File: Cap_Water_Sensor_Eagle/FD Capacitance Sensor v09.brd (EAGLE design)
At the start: 35.1 x 27.6 mm, 17 parts, among them U1 NTS4101PT1, U2 TLC555CD

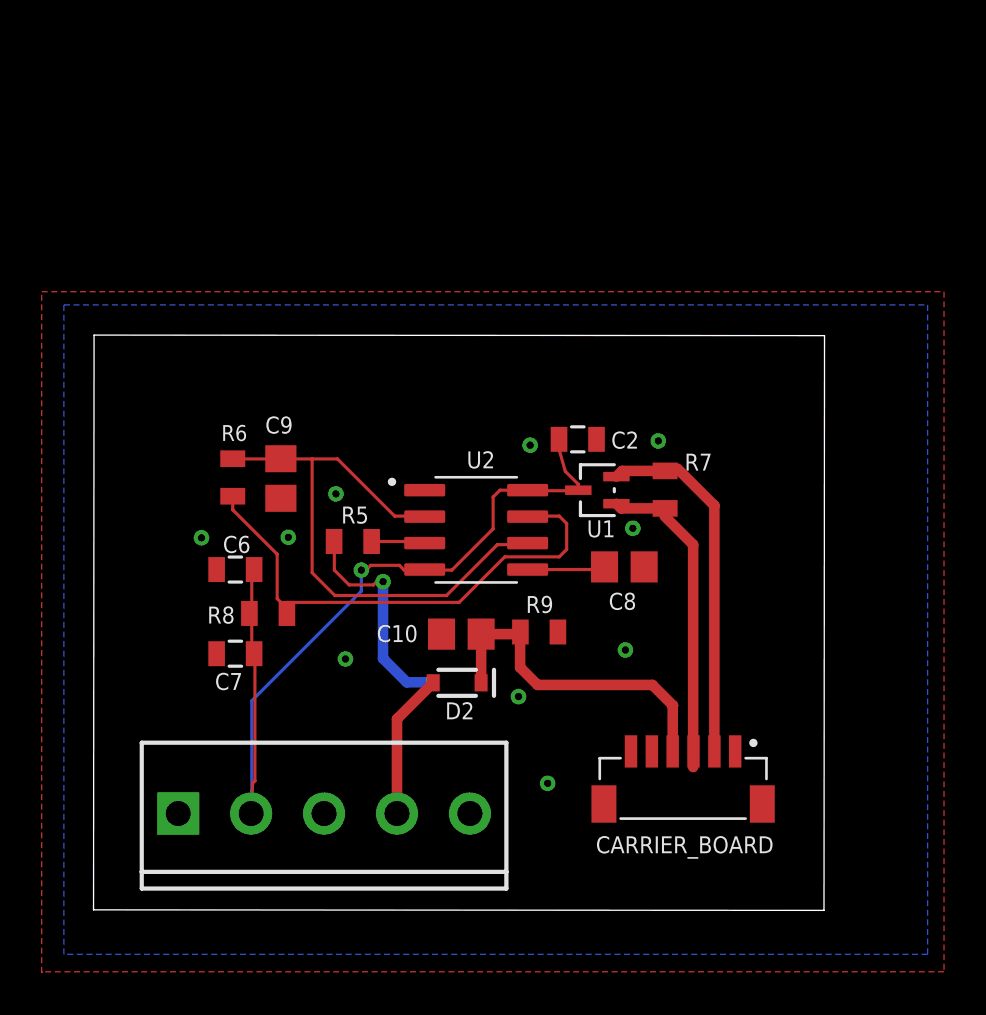
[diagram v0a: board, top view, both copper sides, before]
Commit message: Version 9 with board dimensions
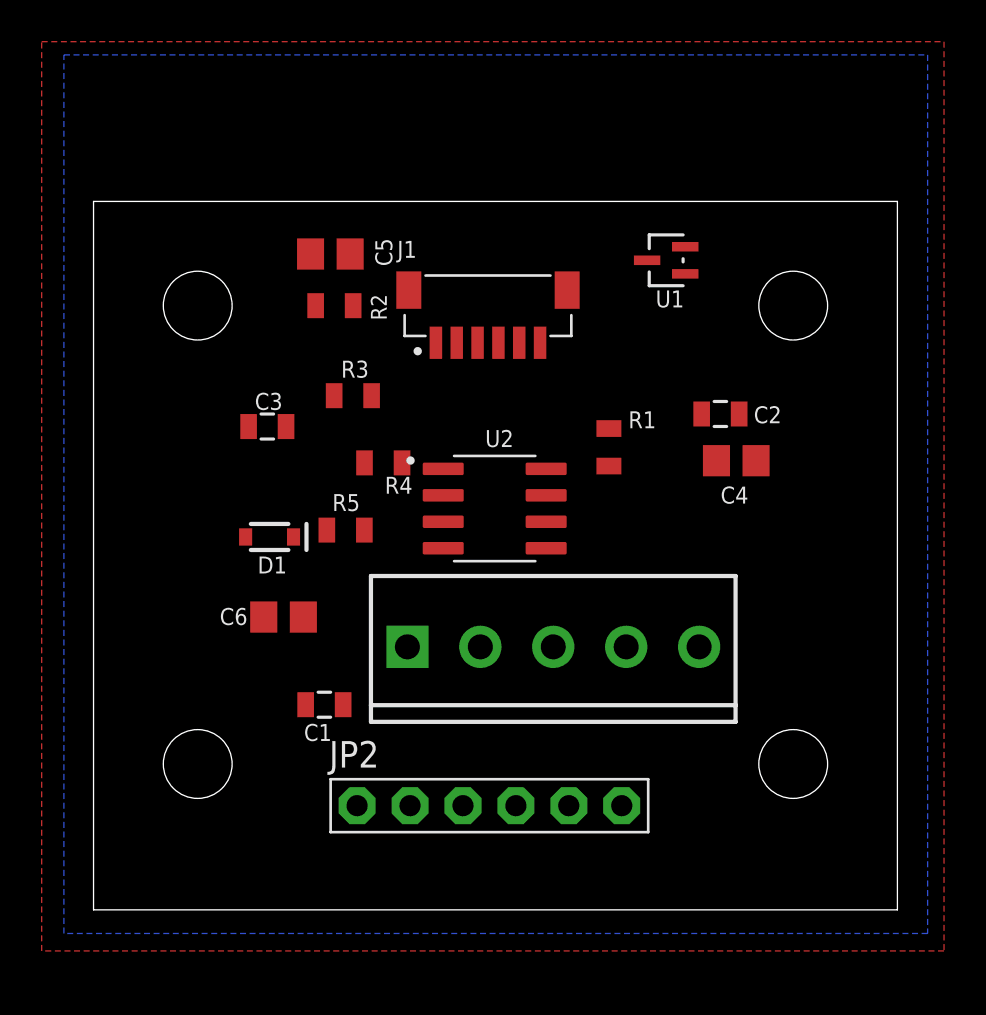
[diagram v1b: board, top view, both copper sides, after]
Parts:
- removed C10: 1uF, rcl:C0805
- removed C7: 0.1uF, Custom Components:0805@1
- removed C8: 10nf, rcl:C0805
- removed C9: 470pf, rcl:C0805
- removed CARRIER_BOARD: BM06B-SRSS-TBT(LF)(SN), Custom Components:JST_BM06B-SRSS-TB(LF)(SN)
- removed D2: 250mA/100V, Custom Components:SOD-323
- removed FRAME1: FRAME-LETTERNO_PACKAGE, SparkFun-Aesthetics:DUMMY
- removed R6: 1k, Custom Components:0805
- removed R7: 100k, Custom Components:0805
- removed R8: 330, Custom Components:0805
- removed R9: 1M, Custom Components:0805
- added C1: 0.1uF, Custom Components:0805@1
- added C3: 10nF, Custom Components:0805@1
- added C4: 10nf, rcl:C0805
- added C5: 470pf, rcl:C0805
- added D1: 250mA/100V, Custom Components:SOD-323
- added J2: (no value), SparkFun-Connectors:SCREWTERMINAL-3.5MM-5
- added JP2: (no value), adafruit:1X06-BIG
- added R1: 100k, Custom Components:0805
- added R2: 1k, Custom Components:0805
- added R3: 10k, Custom Components:0805
- added R4: 330, Custom Components:0805
- added U$1, U$2, U$3, U$4: STAND-OFF, SparkFun-Hardware:STAND-OFF
- C6: value 10nF -> 1uF; device Custom Components:0805@1 -> rcl:C0805
- J1: value (none) -> BM06B-SRSS-TBT(LF)(SN); device SparkFun-Connectors:SCREWTERMINAL-3.5MM-5 -> Custom Components:JST_BM06B-SRSS-TB(LF)(SN)
- R5: value 10k -> 1M
- moved J1 29.2 mm to (18.9, 29.7)
- moved U1 11.5 mm to (27.5, 31.2)
- moved C2 6.95 mm to (30.1, 23.8)
- moved C6 3.25 mm to (9.12, 14.1), turned to 0 degrees
- moved U2 1.36 mm to (19.3, 19.3)
- moved R5 0.65 mm to (12.1, 18.2)
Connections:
- new net N$2: JP2.3
- new net N$3: JP2.2
- new net N$4: JP2.4
- new net N$6: JP2.5
- net !EN: now also J1.3, R1.1; no longer CARRIER_BOARD.3, R7.1
- net +3V3: now also J1.2, R1.2; no longer CARRIER_BOARD.2, R7.2
- net GND: now also C1.2, C3.2, C4.1, C5.1, C6.1, J1.S1, J1.S2, J2.1, JP2.1, R5.1; no longer C10.1, C6.2, C7.2, C8.1, C9.1, CARRIER_BOARD.1, CARRIER_BOARD.S1, CARRIER_BOARD.S2, R9.1
- net N$1: now also C4.2; no longer C8.2
- net N$5: now also R3.1; no longer R5.1
- net N$8: now also C5.2, R2.1; no longer C9.2, R6.1
- net N$9: now also R2.2, R4.1; no longer R6.2, R8.1
- net NC: now also J1.6; no longer CARRIER_BOARD.6
- net OUTPUT1: now also C6.2, D1.C, J1.4, R5.2; no longer C10.2, CARRIER_BOARD.4, D2.C, R9.2
- net OUTPUT2: now also J1.5; no longer CARRIER_BOARD.5
- net SENSOR1: now also D1.A, J2.4, R3.2; no longer D2.A, J1.4, R5.2
- net SENSOR2: now also J2.5; no longer J1.5
- net SHEILD: now also J2.3; no longer J1.3
- net VCC: now also C1.1, C3.1, J2.2, R4.2; no longer C6.1, C7.1, J1.2, R8.2
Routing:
- net VCC: track 41.8 -> 0.61 mm, vias 1 -> 0
- net N$8: track 27.7 -> 0.26 mm
- net N$9: track 25.0 -> 0.03 mm
- net SENSOR1: track 17.6 -> 0.00 mm, vias 1 -> 0
- net +3V3: track 17.5 -> 0.07 mm
- net !EN: track 16.3 -> 0.03 mm
- net OUTPUT1: track 16.5 -> 0.41 mm
- net N$1: track 3.79 -> 0.03 mm
- net N$5: track 2.58 -> 0.00 mm
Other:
- board size 35.1 x 27.6 mm -> 38.6 x 34 mm

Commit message: Added Auto Routed Lines
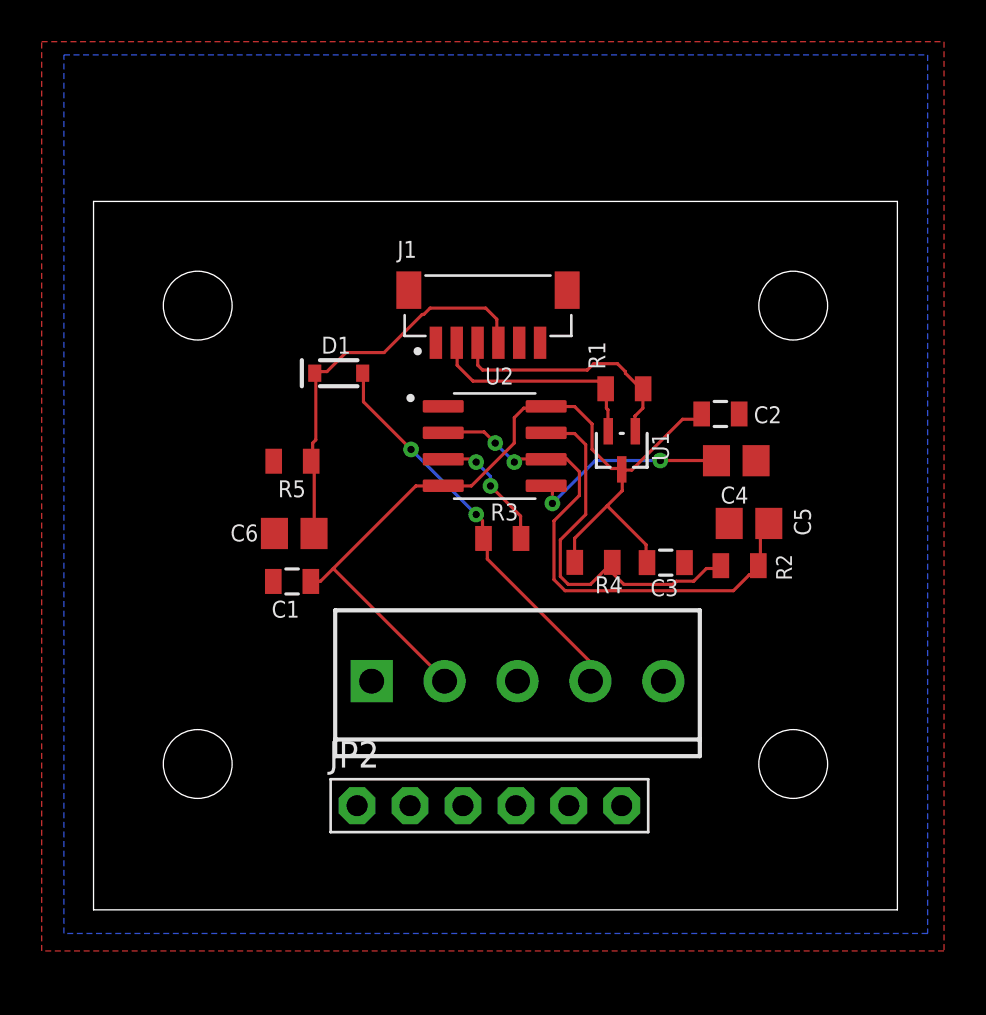
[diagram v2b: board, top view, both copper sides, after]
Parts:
- moved C5 23.9 mm to (31.5, 18.5)
- moved R2 23.1 mm to (31.0, 16.5)
- moved C3 20.2 mm to (27.5, 16.7), turned to 0 degrees
- moved R4 11.2 mm to (24.0, 16.7)
- moved R3 9.92 mm to (19.6, 17.8)
- moved U1 9.37 mm to (25.4, 22.1), turned to 180 degrees
- moved D1 8.53 mm to (11.8, 25.8), turned to 0 degrees
- moved C1 6.12 mm to (9.53, 15.8)
- moved R5 4.17 mm to (9.55, 21.5), turned to 0 degrees
- moved C6 4.04 mm to (9.63, 18.1)
- moved U2 3.00 mm to (19.3, 22.3)
- moved R1 2.91 mm to (25.5, 25.0), turned to 180 degrees
- moved J2 2.38 mm to (13.3, 11.0)
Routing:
- net VCC: track 0.61 -> 43.7 mm
- net N$8: track 0.26 -> 26.2 mm, vias 0 -> 2
- net SENSOR1: track 0.00 -> 19.3 mm, vias 0 -> 2
- net OUTPUT1: track 0.41 -> 19.5 mm
- net N$9: track 0.03 -> 18.4 mm
- net !EN: track 0.03 -> 12.0 mm
- net +3V3: track 0.07 -> 10.8 mm
- net N$1: track 0.03 -> 9.76 mm, vias 0 -> 2
- net N$5: track 0.00 -> 6.21 mm, vias 0 -> 2

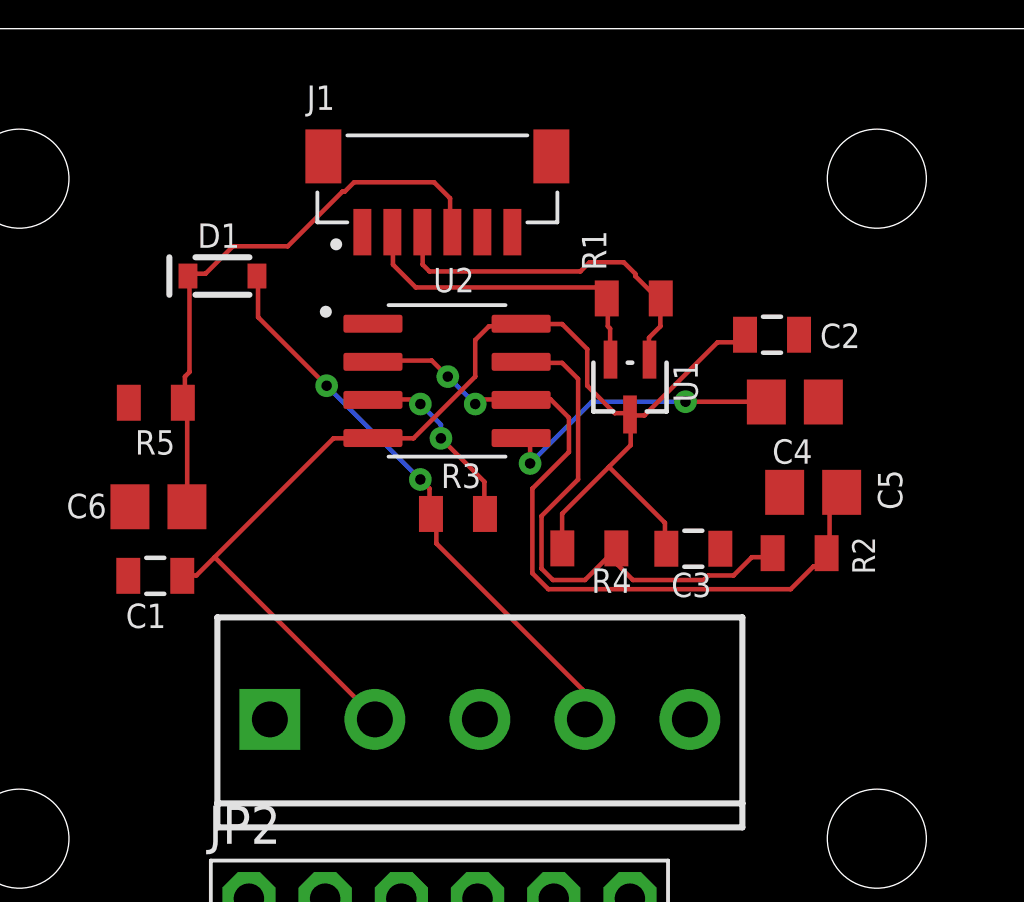
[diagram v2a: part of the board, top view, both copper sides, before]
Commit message: Removed Auto Route
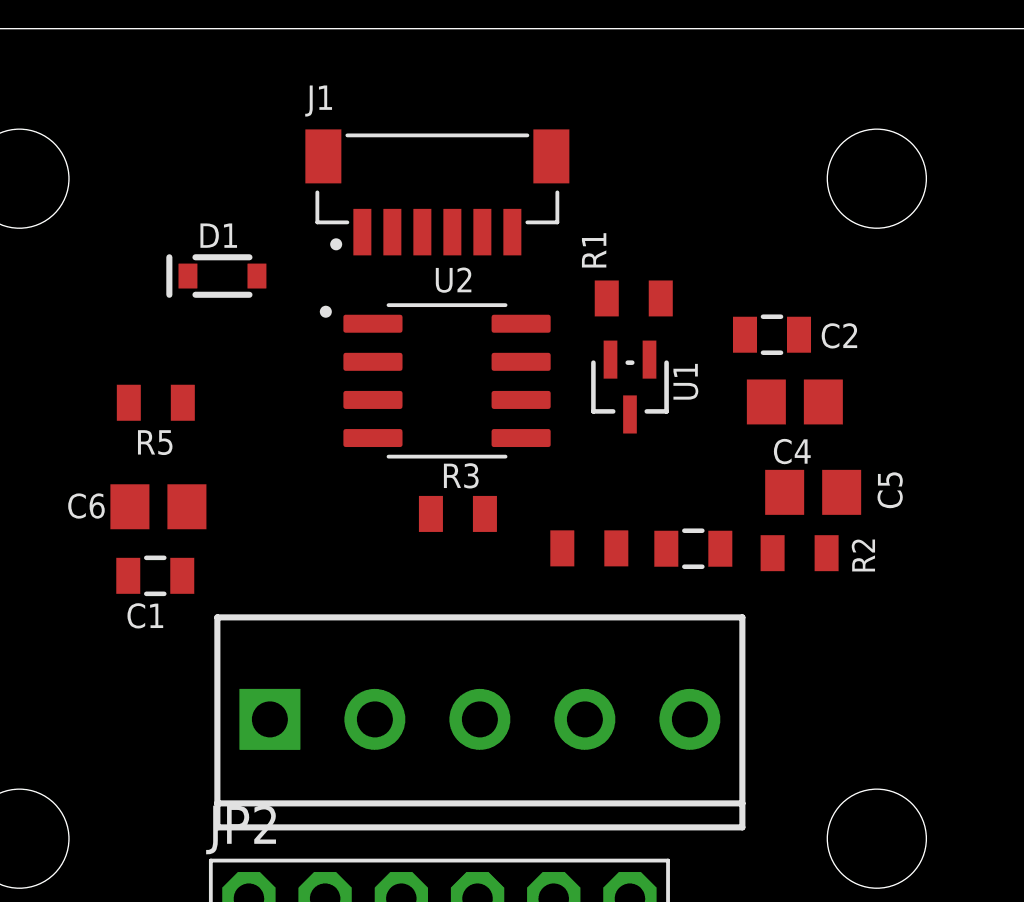
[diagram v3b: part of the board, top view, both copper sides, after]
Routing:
- net VCC: track 43.7 -> 0.00 mm
- net N$8: track 26.2 -> 0.00 mm, vias 2 -> 0
- net OUTPUT1: track 19.5 -> 0.00 mm
- net SENSOR1: track 19.3 -> 0.00 mm, vias 2 -> 0
- net N$9: track 18.4 -> 0.00 mm
- net !EN: track 12.0 -> 0.00 mm
- net +3V3: track 10.8 -> 0.00 mm
- net N$1: track 9.76 -> 0.00 mm, vias 2 -> 0
- net N$5: track 6.21 -> 0.00 mm, vias 2 -> 0
